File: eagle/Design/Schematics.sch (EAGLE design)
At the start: 77 parts, among them IC1 LM1117, IC2 CY7C68013A-56PVXC, IC3 ADS7042DCU, IC4 ADS7042DCU, Q1 SI2369DS, Q2 24MHz, X1 MPT2, X10 MPT3, X11 MPT2, X12 MPT2, X13 MPT2, X14 MPT2, X15 MPT2, X16 MPT2, X2 PN61729-S, X3 MPT2, X4 MPT2, X5 MPT2, X6 MPT2, X7 MPT2, X8 MPT2, X9 MPT3

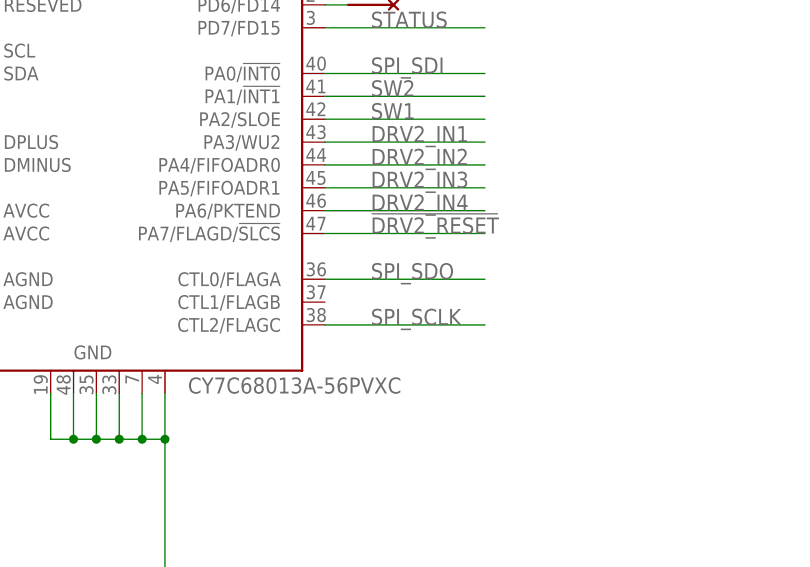
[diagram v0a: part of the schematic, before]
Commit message: Routed nets for Temp Sensor #1.
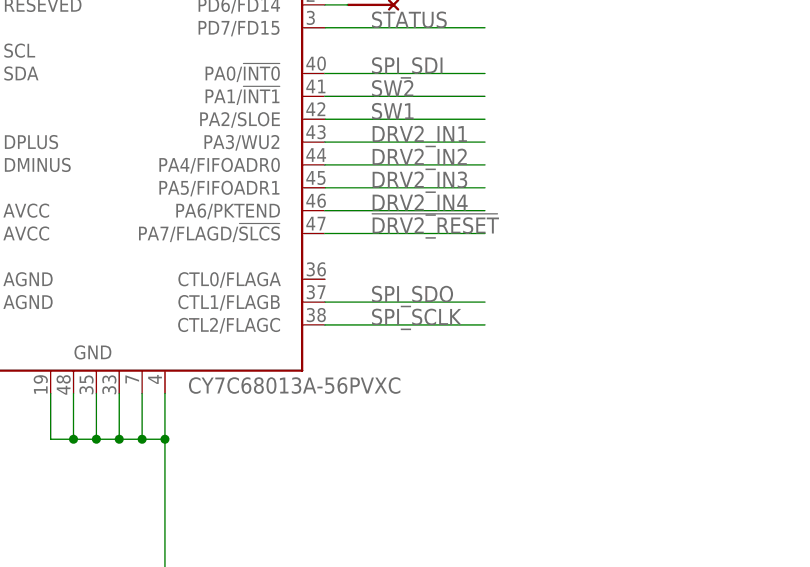
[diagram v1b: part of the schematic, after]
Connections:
- net SPI_SDO: now also IC2.CTL1/FLAGB; no longer IC2.CTL0/FLAGA
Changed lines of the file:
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@@
-</segment>
-<segment>
-<pinref part="IC2" gate="G$1" pin="CTL0/FLAGA"/>
-<wire x1="-406.4" y1="-284.48" x2="-388.62" y2="-284.48" width="0.1524" layer="91"/>
-<label x="-401.32" y="-284.48" size="1.778" layer="95"/>
 </segment>
 <segment>
@@
 <label x="-289.56" y="-73.66" size="1.778" layer="95"/>
 </segment>
+<segment>
+<pinref part="IC2" gate="G$1" pin="CTL1/FLAGB"/>
+<wire x1="-406.4" y1="-287.02" x2="-388.62" y2="-287.02" width="0.1524" layer="91"/>
+<label x="-401.32" y="-287.02" size="1.778" layer="95"/>
+</segment>
 </net>

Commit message: Goodbye USB, hello Pi
Completely changed the direction of the hardware development.
Originally wanted to utilize a USB interface to plug into any PC but
found it was easier (and cheaper) to by a Raspberry Pi for $35 and build
an expansion board to control the brew hardware.  Created a barebone set
of schematics and layout.
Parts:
- removed C12, C18: 200n, resistor:C-USC0603
- removed C13, C19, C20, C21: 100n, resistor:C-USC0603
- removed C22, C23: 1u, resistor:C-USC0603
- removed C3, C7: .1u, resistor:C-USC0603
- removed C4, C5: 27p, resistor:C-USC0603
- removed C6: 2.2u, resistor:C-USC0603
- removed IC2: CY7C68013A-56PVXC, cypress:CY7C68013A-56PVXC
- removed IC3, IC4: ADS7042DCU, texas:ADS7042DCU
- removed NC1, NC13, NC14, NC15, NC2, NC3, NC4, NC5, NC7: NC, Common:NC
- removed Q2: 24MHz, crystal:CRYSTALHC18U-V
- removed R10, R9: 390 .1%, resistor:R-US_R0603
- removed R11, R12, R2: 100K, resistor:R-US_R0603
- removed R13, R14: DNS, resistor:R-US_R0603
- removed R3, R4: 22, resistor:R-US_R0603
- removed R5, R6: 2.2K, resistor:R-US_R0603
- removed S1: (no value), switch-omron:10-XX
- removed TS1, TS2: MAX31865, Common:MAX31865
- removed X10, X9: MPT3, Common:MPT3
- removed X15, X16: MPT2, Common:MPT2
- removed X2: PN61729-S, con-berg:PN61729-S
- added PCB: RPI3, Custom:RPI3
- C1: value 10u -> 0.22u
- C2: value 100u -> 0.1u
- IC1: value LM1117 -> LM340S; device Common:LM1117 -> linear:LM340S
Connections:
- removed net !ADC1_CS: IC2.PB2/FD2, IC3.!SC
- removed net !ADC2_CS: IC2.PB1/FD1, IC4.!SC
- removed net !TS1_CS: TS1.!CS
- removed net !TS2_CS: TS2.!CS
- removed net +5V_USB: X2.4
- removed net DMINUS: IC2.DMINUS, R4.2
- removed net DPLUS: IC2.DPLUS, R3.2
- removed net N$1: IC2.SCL, R6.2
- removed net N$11: R10.1, TS2.ISENSOR, TS2.REFIN-
- removed net N$12: IC2.CLKOUT/T1OUT, NC1.P$1
- removed net N$14: IC3.AINP, R11.2
- removed net N$15: R10.2, TS2.BIAS, TS2.REFIN+
- removed net N$16: C20.1, R11.1, X15.P$1
- removed net N$17: TS2.FORCE+, TS2.FORCE2, X10.P$1
- removed net N$18: C19.2, TS2.FORCE-, TS2.RTDIN-, X10.P$3
- removed net N$19: C19.1, TS2.RTDIN+, X10.P$2
- removed net N$2: IC2.SDA, R5.2
- removed net N$20: NC5.P$1, TS1.!DRDY
- removed net N$21: NC7.P$1, TS2.!DRDY
- removed net N$3: R4.1, X2.2
- removed net N$36: IC2.RDY0/SLRD, NC2.P$1
- removed net N$37: IC2.RDY1/SLRW, NC3.P$1
- removed net N$38: IC2.IFCLK/T0OUT, NC4.P$1
- removed net N$4: R3.1, X2.3
- removed net N$40: IC4.AINP, R12.2
- removed net N$45: C13.2, TS1.FORCE-, TS1.RTDIN-, X9.P$3
- removed net N$46: C21.1, R12.1, X16.P$1
- removed net N$48: C20.2, IC3.AINM, R14.1, X15.P$2
- removed net N$49: C21.2, IC4.AINM, R13.1, X16.P$2
- removed net N$5: R9.1, TS1.ISENSOR, TS1.REFIN-
- removed net N$50: IC2.PB0/FD0, NC13.P$1
- removed net N$54: IC2.PD5/FD13, NC14.P$1
- removed net N$55: IC2.PD6/FD14, NC15.P$1
- removed net N$6: R9.2, TS1.BIAS, TS1.REFIN+
- removed net N$7: TS1.FORCE+, TS1.FORCE2, X9.P$1
- removed net N$9: C13.1, TS1.RTDIN+, X9.P$2
- removed net RESETN: C3.1, IC2.!RESET, R2.1, S1.S, S1.S1
- removed net SPI_SCLK: IC2.CTL2/FLAGC, IC3.SCLK, IC4.SCLK, TS1.SCLK, TS2.SCLK
- removed net SPI_SDI: IC2.PA0/!INT0, TS1.SDI, TS2.SDI
- removed net SPI_SDO: IC2.CTL1/FLAGB, IC3.SDO, IC4.SDO, TS1.SDO, TS2.SDO
- removed net XTALIN: C4.1, IC2.XTALIN, Q2.1
- removed net XTALOUT: C5.1, IC2.XTALOUT, Q2.2
- new net +5V: C2.1, IC1.OUT, PCB-PWR.5V@2, PCB-PWR.5V@4
- net !DRV1_RESET: no longer IC2.PD4/FD12
- net !DRV2_RESET: no longer IC2.PA7/FLAGD/!SLCS
- net +3P3V: now also PCB-PWR.3V3@1, PCB-PWR.3V3@17; no longer C12.1, C18.1, C2.1, C22.1, C23.1, C6.1, C7.1, IC1.VOUT, IC2.AVCC, IC2.AVCC@1, IC2.VCC, IC2.VCC@1, IC2.VCC@2, IC2.VCC@3, IC2.VCC@4, IC2.VCC@5, IC2.WAKEUP, IC3.VDDA, IC3.VDDD, IC4.VDDA, IC4.VDDD, R2.2, R5.1, R6.1, TS1.DVDD, TS1.VDD, TS2.DVDD, TS2.VDD
- net DRV1_IN1: no longer IC2.PD0/FD8
- net DRV1_IN2: no longer IC2.PD1/FD9
- net DRV1_IN3: no longer IC2.PD2/FD10
- net DRV1_IN4: no longer IC2.PD3/FD11
- net DRV2_IN1: no longer IC2.PA3/WU2
- net DRV2_IN2: no longer IC2.PA4/FIFOADR0
- net DRV2_IN3: no longer IC2.PA5/FIFOADR1
- net DRV2_IN4: no longer IC2.PA6/PKTEND
- net GND: now also IC1.GND@1, IC1.GND@2, PCB-PWR.GND@14, PCB-PWR.GND@20, PCB-PWR.GND@25, PCB-PWR.GND@30, PCB-PWR.GND@34, PCB-PWR.GND@39, PCB-PWR.GND@6, PCB-PWR.GND@9; no longer C12.2, C18.2, C22.2, C23.2, C3.2, C4.2, C5.2, C6.2, C7.2, IC1.GND, IC2.AGND, IC2.AGND@1, IC2.GND, IC2.GND@1, IC2.GND@2, IC2.GND@3, IC2.GND@4, IC2.GND@5, IC2.RESEVED, IC3.GND, IC4.GND, R13.2, R14.2, S1.P, S1.P1, TS1.DGND, TS1.GND1, TS1.GND2, TS2.DGND, TS2.GND1, TS2.GND2, X2.1, X2.S1, X2.S2
- net N$13: now also IC1.IN; no longer IC1.VIN
- net STATUS: no longer IC2.PD7/FD15
- net SW1: no longer IC2.PA2/SLOE
- net SW2: no longer IC2.PA1/!INT1
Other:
- note removed: "12bit ADC circuits optimized for DC sensor applications like temperature, volume, etc..."
- note removed: "Analog-to-Digital Converter"
- note removed: "Configured for 3 wire RTD100 temperature probes."
- note removed: "Configured to drive 12V SSRs and 12V normally closed motorized ball vavles."
- note removed: "Drivers"
- note removed: "Microcontroller"
- note removed: "Miscellanous"
- note removed: "Power"
- note removed: "Temperature Sensors"
- moved on the sheet: C1, C10, C11, C14, C15, C16, C17, C2, C8, C9, DRV1, DRV2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
